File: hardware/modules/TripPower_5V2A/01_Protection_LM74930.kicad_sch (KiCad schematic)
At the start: 38 parts, among them J301 INPUT: VIN/RUN/GND, J302 OUT: PROT_UNFUSED/5V/GND, Q301 SQM10250E_GE3 250V CANDIDATE, Q302 BUK7Y4R8-60EX 60V CANDIDATE, U301 LM74930QRGERQ1

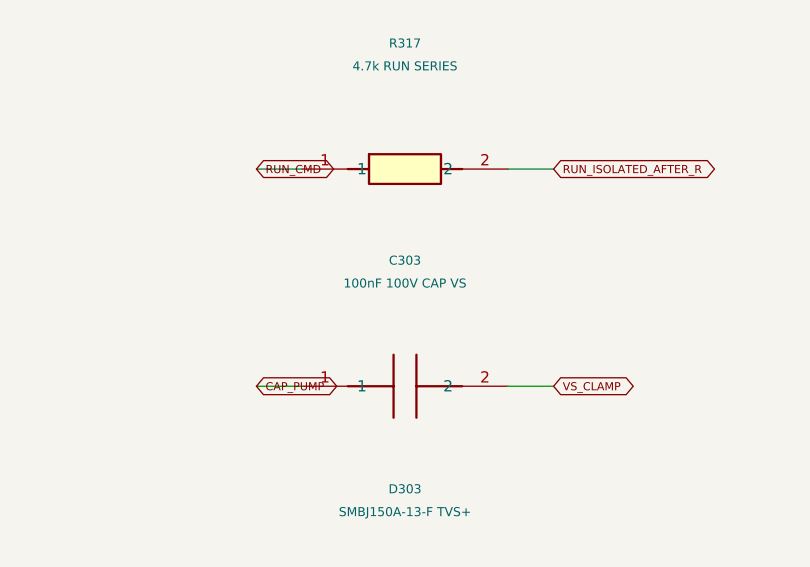
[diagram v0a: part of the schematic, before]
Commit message: feat(TripPower): select automotive 470nF 100V X7R CAP-VS C303 with 1206 KiCad footprint
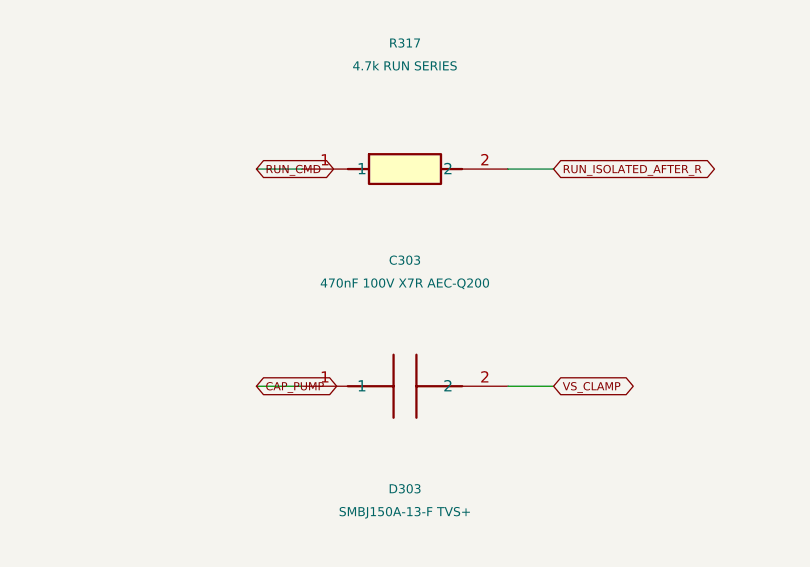
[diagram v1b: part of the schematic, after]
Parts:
- C303: value 100nF 100V CAP VS -> 470nF 100V X7R AEC-Q200; footprint Tripmaster:C_1206_3216 -> Capacitor_SMD:C_1206_3216Metric; Alternative_MPN (none) -> CGA5L2X7R2A474K160AA; MPN (none) -> C1206C474K1RECAUTO7210; Supplier_URL (none) -> https://www.mouser.de/de/ProductDetail/KEMET/C1206C474K1REC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
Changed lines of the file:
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@@
 (symbol (lib_id "Tripmaster_Sym:C") (at 234.95 299.72 0) (unit 1) (in_bom yes) (on_board yes) (dnp no) (property "Reference" "C301" (at 234.95 285.75 0) (effects (font (size 1 1)))) (property "Value" "47nF 50V TMR" (at 234.95 288.29 0) (effects (font (size 1 1)))) (property "Footprint" "Tripmaster:C_1206_3216" (at 234.95 299.72 0) (effects (font (size 1.0 1.0)) (hide yes))) (pin "1") (pin "2") (instances (project "TripPower_5V2A" (path "/f1512578-cc72-4c26-bf70-dbbd00000001/f1512578-cc72-4c26-bf70-dbbd00000002" (reference "C301") (unit 1)))))
 (symbol (lib_id "Tripmaster_Sym:C") (at 320.04 299.72 0) (unit 1) (in_bom yes) (on_board yes) (dnp no) (property "Reference" "C302" (at 320.04 285.75 0) (effects (font (size 1 1)))) (property "Value" "1uF 100V VS CLAMP" (at 320.04 288.29 0) (effects (font (size 1 1)))) (property "Footprint" "Tripmaster:C_1210_3225" (at 320.04 299.72 0) (effects (font (size 1.0 1.0)) (hide yes))) (pin "1") (pin "2") (instances (project "TripPower_5V2A" (path "/f1512578-cc72-4c26-bf70-dbbd00000001/f1512578-cc72-4c26-bf70-dbbd00000002" (reference "C302") (unit 1)))))
-(symbol (lib_id "Tripmaster_Sym:C") (at 405.13 299.72 0) (unit 1) (in_bom yes) (on_board yes) (dnp no) (property "Reference" "C303" (at 405.13 285.75 0) (effects (font (size 1 1)))) (property "Value" "100nF 100V CAP VS" (at 405.13 288.29 0) (effects (font (size 1 1)))) (property "Footprint" "Tripmaster:C_1206_3216" (at 405.13 299.72 0) (effects (font (size 1.0 1.0)) (hide yes))) (pin "1") (pin "2") (instances (project "TripPower_5V2A" (path "/f1512578-cc72-4c26-bf70-dbbd00000001/f1512578-cc72-4c26-bf70-dbbd00000002" (reference "C303") (unit 1)))))
+(symbol (lib_id "Tripmaster_Sym:C") (at 405.13 299.72 0) (unit 1) (in_bom yes) (on_board yes) (dnp no) (property "Reference" "C303" (at 405.13 285.75 0) (effects (font (size 1 1)))) (property "Value" "470nF 100V X7R AEC-Q200" (at 405.13 288.29 0) (effects (font (size 1 1)))) (property "Footprint" "Capacitor_SMD:C_1206_3216Metric" (at 405.13 299.72 0) (effects (font (size 1.0 1.0)) (hide yes))) (property "MPN" "C1206C474K1RECAUTO7210" (at 0 0 0) (effects (font (size 1 1)) (hide yes))) (property "Supplier_URL" "https://www.mouser.de/de/ProductDetail/KEMET/C1206C474K1RECAUTO7210" (at 0 0 0) (effects (font (size 1 1)) (hide yes))) (property "Alternative_MPN" "CGA5L2X7R2A474K160AA" (at 0 0 0) (effects (font (size 1 1)) (hide yes))) (pin "1") (pin "2") (instances (project "TripPower_5V2A" (path "/f1512578-cc72-4c26-bf70-dbbd00000001/f1512578-cc72-4c26-bf70-dbbd00000002" (reference "C303") (unit 1)))))
 (symbol (lib_id "Tripmaster_Sym:C") (at 490.22 299.72 0) (unit 1) (in_bom yes) (on_board yes) (dnp no) (property "Reference" "C304" (at 490.22 285.75 0) (effects (font (size 1 1)))) (property "Value" "1uF 100V A BYPASS" (at 490.22 288.29 0) (effects (font (size 1 1)))) (property "Footprint" "Tripmaster:C_1206_3216" (at 490.22 299.72 0) (effects (font (size 1.0 1.0)) (hide yes))) (pin "1") (pin "2") (instances (project "TripPower_5V2A" (path "/f1512578-cc72-4c26-bf70-dbbd00000001/f1512578-cc72-4c26-bf70-dbbd00000002" (reference "C304") (unit 1)))))
 (symbol (lib_id "Tripmaster_Sym:C") (at 64.77 325.12 0) (unit 1) (in_bom yes) (on_board yes) (dnp no) (property "Reference" "C305" (at 64.77 311.15 0) (effects (font (size 1 1)))) (property "Value" "100nF 250V VIN HF" (at 64.77 313.69 0) (effects (font (size 1 1)))) (property "Footprint" "Tripmaster:C_1210_3225" (at 64.77 325.12 0) (effects (font (size 1.0 1.0)) (hide yes))) (pin "1") (pin "2") (instances (project "TripPower_5V2A" (path "/f1512578-cc72-4c26-bf70-dbbd00000001/f1512578-cc72-4c26-bf70-dbbd00000002" (reference "C305") (unit 1)))))

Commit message: feat(TripPower): add passive VS reservoir and EN delay option A prototype candidates
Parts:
- added C308: 10uF 100V VS STARTUP RESERVOIR WIP, Capacitor_SMD:CP_Elec_8x10.5, symbol TripTracer_V1:PWR_CPOL
- added C309: 10uF 50V EN DELAY WIP, Capacitor_SMD:C_1210_3225Metric, symbol Tripmaster_Sym:C
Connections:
- net CTRL_EN: now also C309.1
- net GND: now also C309.2
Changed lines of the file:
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@@
 (wire (pts (xy 161.29 350.52) (xy 166.37 350.52)) (stroke (width 0) (type default)))
 (global_label "GND" (shape bidirectional) (at 166.37 350.52 0) (effects (font (size 0.9 0.9)) (justify left)))
+(symbol (lib_id "TripTracer_V1:PWR_CPOL") (at 320.04 350.52 0) (unit 1) (in_bom yes) (on_board yes) (dnp no) (property "Reference" "C308" (at 320.04 336.55 0) (effects (font (size 1 1)))) (property "Value" "10uF 100V VS STARTUP RESERVOIR WIP" (at 320.04 339.09 0) (effects (font (size 1 1)))) (property "Footprint" "Capacitor_SMD:CP_Elec_8x10.5" (at 320.04 350.52 0) (effects (font (size 1.0 1.0)) (hide yes))) (property "MPN" "EEE-TG2A100P" (at 0 0 0) (effects (font (size 1 1)) (hide yes))) (property "Supplier_URL" "https://www.digikey.de/en/products/detail/panasonic-industry/EEE-TG2A100P/817792" (at 0 0 0) (effects (font (size 1 1)) (hide yes))) (pin "1") (pin "2") (instances (project "TripPower_5V2A" (path "/f1512578-cc72-4c26-bf70-dbbd00000001/f1512578-cc72-4c26-bf70-dbbd00000002" (reference "C308") (unit 1)))))
+(wire (pts (xy 308.61 350.52) (xy 303.53 350.52)) (stroke (width 0) (type default)))
+(global_label "VS_CLAMP" (shape bidirectional) (at 303.53 350.52 0) (effects (font (size 0.9 0.9)) (justify left)))
+(wire (pts (xy 331.47 350.52) (xy 336.55 350.52)) (stroke (width 0) (type default)))
+(global_label "GND" (shape bidirectional) (at 336.55 350.52 0) (effects (font (size 0.9 0.9)) (justify left)))
+(symbol (lib_id "Tripmaster_Sym:C") (at 405.13 350.52 0) (unit 1) (in_bom yes) (on_board yes) (dnp no) (property "Reference" "C309" (at 405.13 336.55 0) (effects (font (size 1 1)))) (property "Value" "10uF 50V EN DELAY WIP" (at 405.13 339.09 0) (effects (font (size 1 1)))) (property "Footprint" "Capacitor_SMD:C_1210_3225Metric" (at 405.13 350.52 0) (effects (font (size 1.0 1.0)) (hide yes))) (property "MPN" "12105C106K4T2A" (at 0 0 0) (effects (font (size 1 1)) (hide yes))) (property "Supplier_URL" "https://www.mouser.de/de/ProductDetail/KEMET/12105C106K4T2A" (at 0 0 0) (effects (font (size 1 1)) (hide yes))) (property "Status" "AUTO_EN_ONLY; RUN_CMD bypass not yet gated" (at 0 0 0) (effects (font (size 1 1)) (hide yes))) (pin "1") (pin "2") (instances (project "TripPower_5V2A" (path "/f1512578-cc72-4c26-bf70-dbbd00000001/f1512578-cc72-4c26-bf70-dbbd00000002" (reference "C309") (unit 1)))))
+(wire (pts (xy 393.7 350.52) (xy 388.62 350.52)) (stroke (width 0) (type default)))
+(global_label "CTRL_EN" (shape bidirectional) (at 388.62 350.52 0) (effects (font (size 0.9 0.9)) (justify left)))
+(wire (pts (xy 416.56 350.52) (xy 421.64 350.52)) (stroke (width 0) (type default)))
+(global_label "GND" (shape bidirectional) (at 421.64 350.52 0) (effects (font (size 0.9 0.9)) (justify left)))
  (embedded_fonts no))

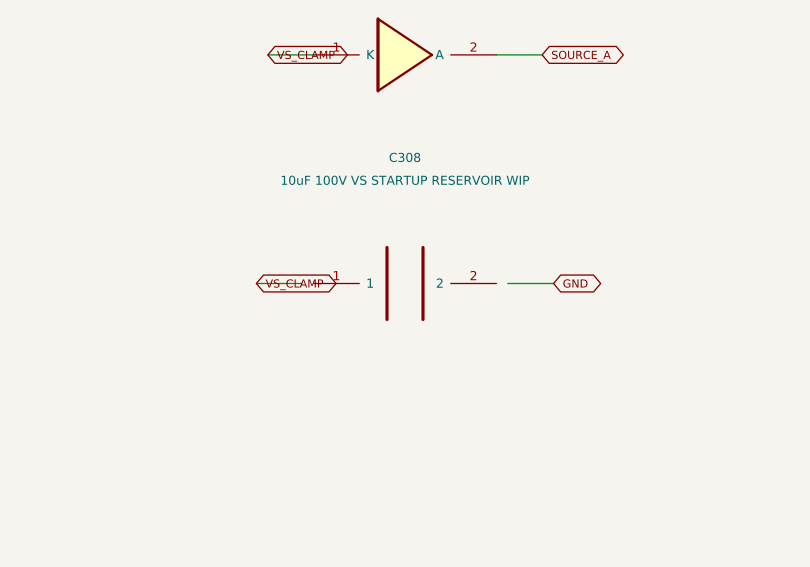
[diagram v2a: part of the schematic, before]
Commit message: fix(TripPower): snap C308 electrolytic wires to real ±10.16mm PWR_CPOL pin endpoints
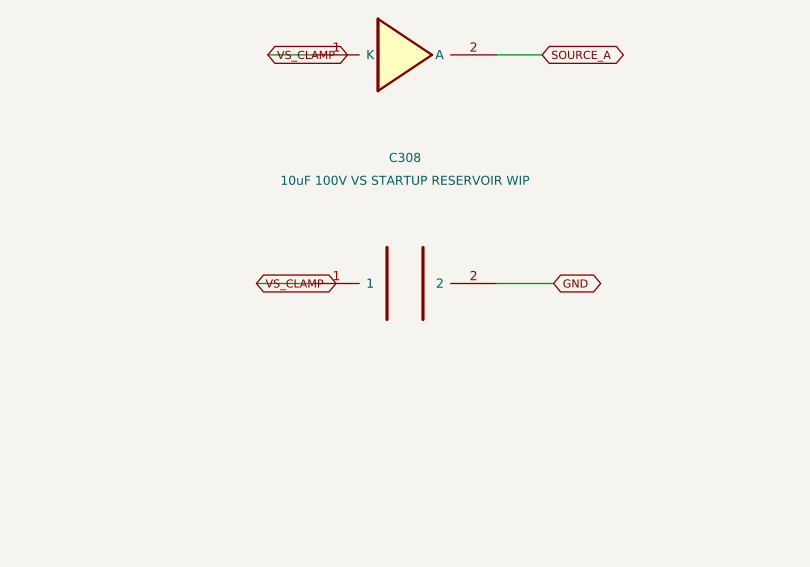
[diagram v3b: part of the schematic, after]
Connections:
- net GND: now also C308.2
- net VS_CLAMP: now also C308.1
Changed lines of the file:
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@@
 (global_label "GND" (shape bidirectional) (at 166.37 350.52 0) (effects (font (size 0.9 0.9)) (justify left)))
 (symbol (lib_id "TripTracer_V1:PWR_CPOL") (at 320.04 350.52 0) (unit 1) (in_bom yes) (on_board yes) (dnp no) (property "Reference" "C308" (at 320.04 336.55 0) (effects (font (size 1 1)))) (property "Value" "10uF 100V VS STARTUP RESERVOIR WIP" (at 320.04 339.09 0) (effects (font (size 1 1)))) (property "Footprint" "Capacitor_SMD:CP_Elec_8x10.5" (at 320.04 350.52 0) (effects (font (size 1.0 1.0)) (hide yes))) (property "MPN" "EEE-TG2A100P" (at 0 0 0) (effects (font (size 1 1)) (hide yes))) (property "Supplier_URL" "https://www.digikey.de/en/products/detail/panasonic-industry/EEE-TG2A100P/817792" (at 0 0 0) (effects (font (size 1 1)) (hide yes))) (pin "1") (pin "2") (instances (project "TripPower_5V2A" (path "/f1512578-cc72-4c26-bf70-dbbd00000001/f1512578-cc72-4c26-bf70-dbbd00000002" (reference "C308") (unit 1)))))
-(wire (pts (xy 308.61 350.52) (xy 303.53 350.52)) (stroke (width 0) (type default)))
+(wire (pts (xy 309.88 350.52) (xy 303.53 350.52)) (stroke (width 0) (type default)))
 (global_label "VS_CLAMP" (shape bidirectional) (at 303.53 350.52 0) (effects (font (size 0.9 0.9)) (justify left)))
-(wire (pts (xy 331.47 350.52) (xy 336.55 350.52)) (stroke (width 0) (type default)))
+(wire (pts (xy 330.2 350.52) (xy 336.55 350.52)) (stroke (width 0) (type default)))
 (global_label "GND" (shape bidirectional) (at 336.55 350.52 0) (effects (font (size 0.9 0.9)) (justify left)))
 (symbol (lib_id "Tripmaster_Sym:C") (at 405.13 350.52 0) (unit 1) (in_bom yes) (on_board yes) (dnp no) (property "Reference" "C309" (at 405.13 336.55 0) (effects (font (size 1 1)))) (property "Value" "10uF 50V EN DELAY WIP" (at 405.13 339.09 0) (effects (font (size 1 1)))) (property "Footprint" "Capacitor_SMD:C_1210_3225Metric" (at 405.13 350.52 0) (effects (font (size 1.0 1.0)) (hide yes))) (property "MPN" "12105C106K4T2A" (at 0 0 0) (effects (font (size 1 1)) (hide yes))) (property "Supplier_URL" "https://www.mouser.de/de/ProductDetail/KEMET/12105C106K4T2A" (at 0 0 0) (effects (font (size 1 1)) (hide yes))) (property "Status" "AUTO_EN_ONLY; RUN_CMD bypass not yet gated" (at 0 0 0) (effects (font (size 1 1)) (hide yes))) (pin "1") (pin "2") (instances (project "TripPower_5V2A" (path "/f1512578-cc72-4c26-bf70-dbbd00000001/f1512578-cc72-4c26-bf70-dbbd00000002" (reference "C309") (unit 1)))))
